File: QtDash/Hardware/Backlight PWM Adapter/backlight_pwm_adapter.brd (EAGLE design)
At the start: 40.4 x 19.5 mm, 9 parts, among them Q1 310mA/60V/1.6Ω, Q2 310mA/60V/1.6Ω

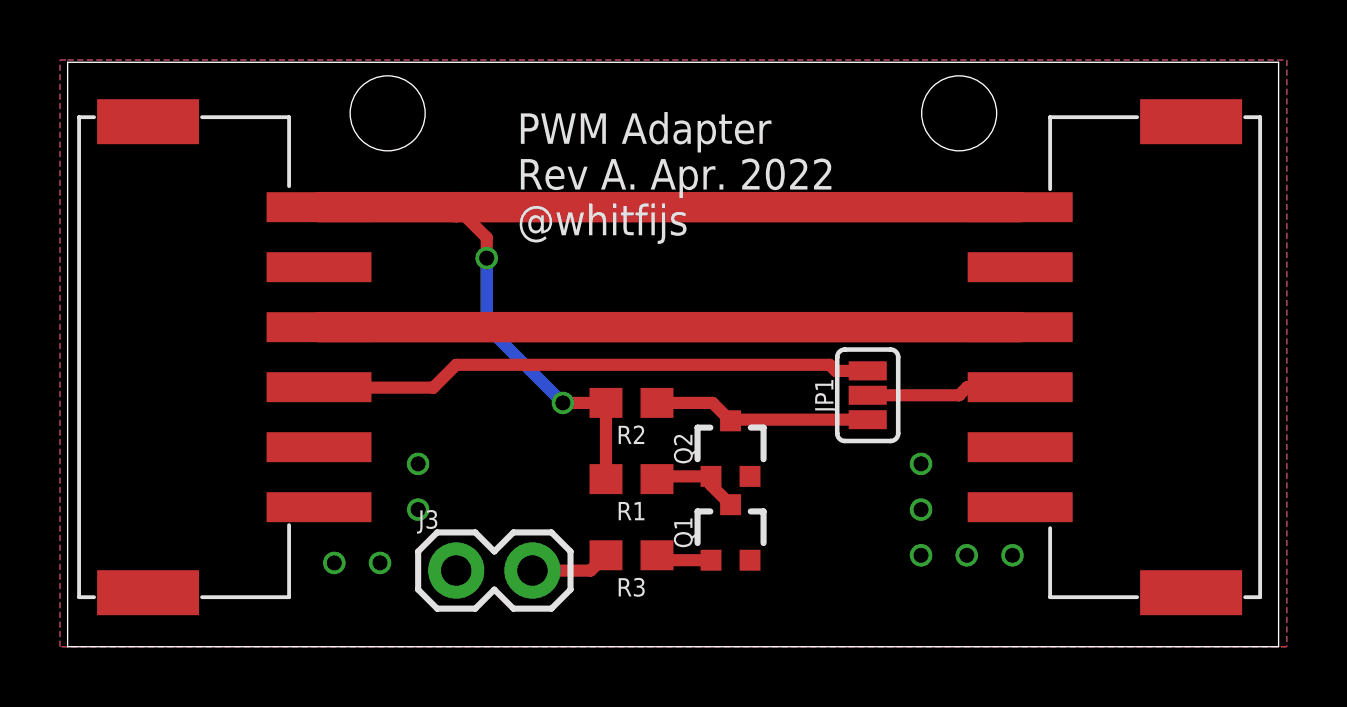
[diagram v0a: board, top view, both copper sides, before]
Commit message: topic/backlight-pwm-control: 	- changed PWM frequency to 30kHz 	- renamed pwm.hpp -> pwm.h 	- started on rev b of PWM adapter board -- pwm signal used directly on EN pin of the OCX OC6700.  There is brightness control that is done outside of the backlight as well that I can't control with the PWM alone.
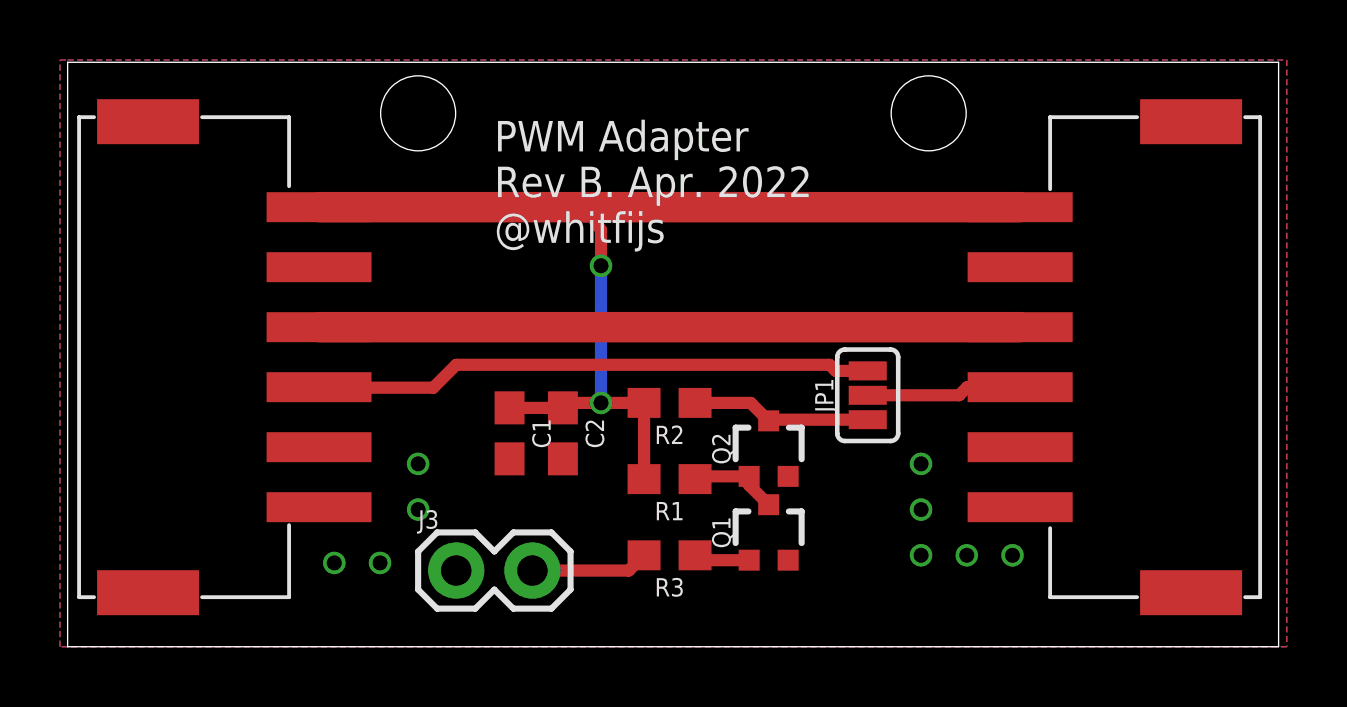
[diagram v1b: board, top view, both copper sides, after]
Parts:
- added C1: 100n, digital_dash:0603
- added C2: 1u, digital_dash:0603
- moved Q1 1.27 mm to (23.6, 3.81)
- moved Q2 1.27 mm to (23.6, 6.60)
- moved R1 1.27 mm to (20.3, 5.59)
- moved R2 1.27 mm to (20.3, 8.13)
- moved R3 1.27 mm to (20.3, 3.05)
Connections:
- net 5V: now also C1.1, C2.1
- net GND: now also C1.2, C2.2
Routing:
- net 5V: track 35.3 -> 37.2 mm
- net PI_PWM_OUT: track 7.29 -> 6.02 mm
- net N$1: track 2.66 -> 3.93 mm
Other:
- board text added: "PWM Adapter Rev B. Apr. 2022 @whitfijs"
- board text removed: "PWM Adapter Rev A. Apr. 2022 @whitfijs"
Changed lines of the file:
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@@
 <setting verticaltext="up"/>
 </settings>
-<grid distance="10" unitdist="mil" unit="mm" style="lines" multiple="1" display="yes" altdistance="0.025" altunitdist="inch" altunit="inch"/>
+<grid distance="10" unitdist="mil" unit="mil" style="lines" multiple="1" display="yes" altdistance="0.025" altunitdist="inch" altunit="inch"/>
 <layers>
 <layer number="1" name="Top" color="4" fill="1" visible="yes" active="yes"/>
@@
 <wire x1="40.62" y1="19.482" x2="0.254" y2="19.482" width="0" layer="20"/>
 <wire x1="0.254" y1="19.482" x2="0.254" y2="0" width="0" layer="20"/>
-<hole x="10.922" y="17.78" drill="2.5"/>
-<hole x="29.972" y="17.78" drill="2.5"/>
-<circle x="10.922" y="17.78" radius="1.27" width="0.4064" layer="41"/>
-<circle x="10.922" y="17.78" radius="1.27" width="0.4064" layer="42"/>
-<circle x="29.972" y="17.78" radius="1.27" width="0.4064" layer="42"/>
-<circle x="29.972" y="17.78" radius="1.27" width="0.4064" layer="41"/>
-<text x="15.24" y="13.716" size="1.016" layer="21" font="vector" ratio="15">PWM Adapter
-Rev A. Apr. 2022
+<hole x="11.938" y="17.78" drill="2.5"/>
+<hole x="28.956" y="17.78" drill="2.5"/>
+<circle x="11.938" y="17.78" radius="1.27" width="0.4064" layer="41"/>
+<circle x="11.938" y="17.78" radius="1.27" width="0.4064" layer="42"/>
+<circle x="28.956" y="17.78" radius="1.27" width="0.4064" layer="42"/>
+<circle x="28.956" y="17.78" radius="1.27" width="0.4064" layer="41"/>
+<text x="14.478" y="13.462" size="1.016" layer="21" font="vector" ratio="15">PWM Adapter
+Rev B. Apr. 2022
 @whitfijs</text>
 </plain>
@@
 <element name="J2" library="backlight_pwm_adapter" package="140-506-417-060" value="" x="32.004" y="9.652" rot="R270"/>
 <element name="JP1" library="SparkFun-Jumpers" package="SMT-JUMPER_3_NO_SILK" value="JUMPER-SMT_3_NO_SILK" x="26.924" y="8.382" rot="R90"/>
-<element name="Q1" library="SparkFun-DiscreteSemi" package="SOT323" value="310mA/60V/1.6Ω" x="22.352" y="3.81">
-<attribute name="PROD_ID" value="TRANS-11151" x="22.352" y="3.81" size="1.778" layer="27" display="off"/>
+<element name="Q1" library="SparkFun-DiscreteSemi" package="SOT323" value="310mA/60V/1.6Ω" x="23.622" y="3.81">
+<attribute name="PROD_ID" value="TRANS-11151" x="23.622" y="3.81" size="1.778" layer="27" display="off"/>
 </element>
-<element name="Q2" library="SparkFun-DiscreteSemi" package="SOT323" value="310mA/60V/1.6Ω" x="22.352" y="6.604">
-<attribute name="PROD_ID" value="TRANS-11151" x="22.352" y="6.604" size="1.778" layer="27" display="off"/>
+<element name="Q2" library="SparkFun-DiscreteSemi" package="SOT323" value="310mA/60V/1.6Ω" x="23.622" y="6.604">
+<attribute name="PROD_ID" value="TRANS-11151" x="23.622" y="6.604" size="1.778" layer="27" display="off"/>
 </element>
-<element name="R1" library="digital_dash" package="0603" value="1k" x="19.05" y="5.588" rot="R180"/>
-<element name="R2" library="digital_dash" package="0603" value="1k" x="19.05" y="8.128" rot="R180"/>
+<element name="R1" library="digital_dash" package="0603" value="1k" x="20.32" y="5.588" rot="R180"/>
+<element name="R2" library="digital_dash" package="0603" value="1k" x="20.32" y="8.128" rot="R180"/>
 <element name="J3" library="SparkFun-Connectors" package="1X02" value="" x="13.208" y="2.54"/>
-<element name="R3" library="digital_dash" package="0603" value="1k" x="19.05" y="3.048" rot="R180"/>
+<element name="R3" library="digital_dash" package="0603" value="1k" x="20.32" y="3.048" rot="R180"/>
+<element name="C1" library="digital_dash" package="0603" value="100n" x="14.986" y="7.112" rot="R270">
+<attribute name="VOLTAGE" value="50V" x="14.986" y="7.112" size="1.778" layer="27" rot="R270" display="off"/>
+</element>
+<element name="C2" library="digital_dash" package="0603" value="1u" x="16.764" y="7.112" rot="R270">
+<attribute name="VOLTAGE" value="25V" x="16.764" y="7.112" size="1.778" layer="27" rot="R270" display="off"/>
+</element>
 </elements>
 <signals>
@@
 <contactref element="R1" pad="1"/>
 <contactref element="Q1" pad="3"/>
-<wire x1="22.352" y1="4.735" x2="21.702" y2="5.385" width="0.4064" layer="1"/>
-<wire x1="21.702" y1="5.385" x2="21.702" y2="5.679" width="0.4064" layer="1"/>
-<wire x1="19.9" y1="5.588" x2="19.991" y2="5.679" width="0.4064" layer="1"/>
-<wire x1="19.991" y1="5.679" x2="21.702" y2="5.679" width="0.4064" layer="1"/>
+<wire x1="23.622" y1="4.735" x2="22.972" y2="5.385" width="0.4064" layer="1"/>
+<wire x1="22.972" y1="5.385" x2="22.972" y2="5.679" width="0.4064" layer="1"/>
+<wire x1="21.17" y1="5.588" x2="21.261" y2="5.679" width="0.4064" layer="1"/>
+<wire x1="21.261" y1="5.679" x2="22.972" y2="5.679" width="0.4064" layer="1"/>
 </signal>
 <signal name="GND">
@@
 <via x="10.668" y="2.794" extent="1-16" drill="0.5"/>
 <via x="9.144" y="2.794" extent="1-16" drill="0.5"/>
+<contactref element="C2" pad="2"/>
+<contactref element="C1" pad="2"/>
 </signal>
 <signal name="PI_PWM_OUT">
@@
 <contactref element="R2" pad="1"/>
 <contactref element="JP1" pad="1"/>
-<wire x1="22.352" y1="7.529" x2="21.753" y2="8.128" width="0.4064" layer="1"/>
-<wire x1="21.753" y1="8.128" x2="19.9" y2="8.128" width="0.4064" layer="1"/>
-<wire x1="22.352" y1="7.529" x2="22.3922" y2="7.5692" width="0.4064" layer="1"/>
-<wire x1="22.3922" y1="7.5692" x2="26.924" y2="7.5692" width="0.4064" layer="1"/>
+<wire x1="23.622" y1="7.529" x2="23.023" y2="8.128" width="0.4064" layer="1"/>
+<wire x1="23.023" y1="8.128" x2="21.17" y2="8.128" width="0.4064" layer="1"/>
+<wire x1="23.622" y1="7.529" x2="23.6622" y2="7.5692" width="0.4064" layer="1"/>
+<wire x1="23.6622" y1="7.5692" x2="26.924" y2="7.5692" width="0.4064" layer="1"/>
 </signal>
 <signal name="5V">
@@
 <contactref element="J2" pad="6"/>
 <contactref element="J1" pad="1"/>
-<wire x1="8.636" y1="14.652" x2="13.208" y2="14.652" width="1.016" layer="1"/>
-<wire x1="13.208" y1="14.652" x2="32.004" y2="14.652" width="1.016" layer="1"/>
-<wire x1="18.2" y1="5.588" x2="18.2" y2="8.128" width="0.4064" layer="1"/>
-<wire x1="18.2" y1="8.128" x2="16.764" y2="8.128" width="0.4064" layer="1"/>
-<via x="16.764" y="8.128" extent="1-16" drill="0.5"/>
-<wire x1="16.764" y1="8.128" x2="14.224" y2="10.668" width="0.4064" layer="16"/>
-<wire x1="14.224" y1="10.668" x2="14.224" y2="12.954" width="0.4064" layer="16"/>
-<via x="14.224" y="12.954" extent="1-16" drill="0.5"/>
-<wire x1="14.224" y1="12.954" x2="14.224" y2="13.636" width="0.4064" layer="1"/>
-<wire x1="14.224" y1="13.636" x2="13.208" y2="14.652" width="0.4064" layer="1"/>
+<wire x1="8.636" y1="14.652" x2="17.526" y2="14.652" width="1.016" layer="1"/>
+<wire x1="17.526" y1="14.652" x2="32.004" y2="14.652" width="1.016" layer="1"/>
+<wire x1="19.47" y1="5.588" x2="19.47" y2="8.128" width="0.4064" layer="1"/>
+<wire x1="19.47" y1="8.128" x2="18.034" y2="8.128" width="0.4064" layer="1"/>
+<via x="18.034" y="8.128" extent="1-16" drill="0.5"/>
+<wire x1="18.034" y1="8.128" x2="18.034" y2="12.7" width="0.4064" layer="16"/>
+<via x="18.034" y="12.7" extent="1-16" drill="0.5"/>
+<wire x1="18.034" y1="12.7" x2="18.034" y2="13.89" width="0.4064" layer="1"/>
+<wire x1="18.034" y1="13.89" x2="17.526" y2="14.652" width="0.4064" layer="1"/>
+<contactref element="C2" pad="1"/>
+<contactref element="C1" pad="1"/>
+<wire x1="18.034" y1="8.128" x2="16.764" y2="8.128" width="0.4064" layer="1"/>
+<wire x1="16.764" y1="8.128" x2="16.764" y2="7.962" width="0.4064" layer="1"/>
+<wire x1="16.764" y1="7.962" x2="14.986" y2="7.962" width="0.4064" layer="1"/>
 </signal>
 <signal name="3.3V">
@@
 <contactref element="J3" pad="2"/>
 <contactref element="R3" pad="2"/>
-<wire x1="15.748" y1="2.54" x2="17.692" y2="2.54" width="0.4064" layer="1"/>
-<wire x1="17.692" y1="2.54" x2="18.2" y2="3.048" width="0.4064" layer="1"/>
+<wire x1="15.748" y1="2.54" x2="18.962" y2="2.54" width="0.4064" layer="1"/>
+<wire x1="18.962" y1="2.54" x2="19.47" y2="3.048" width="0.4064" layer="1"/>
 </signal>
 <signal name="N$2">
 <contactref element="Q1" pad="1"/>
 <contactref element="R3" pad="1"/>
-<wire x1="21.702" y1="2.885" x2="20.063" y2="2.885" width="0.4064" layer="1"/>
-<wire x1="20.063" y1="2.885" x2="19.9" y2="3.048" width="0.4064" layer="1"/>
+<wire x1="22.972" y1="2.885" x2="21.333" y2="2.885" width="0.4064" layer="1"/>
+<wire x1="21.333" y1="2.885" x2="21.17" y2="3.048" width="0.4064" layer="1"/>
 </signal>
 </signals>

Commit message: topic/backlight-pwm-control: 	- added (weak) pullup on PWM input to PWM adapter board 	- probably just need to make a backlight driver on the main board
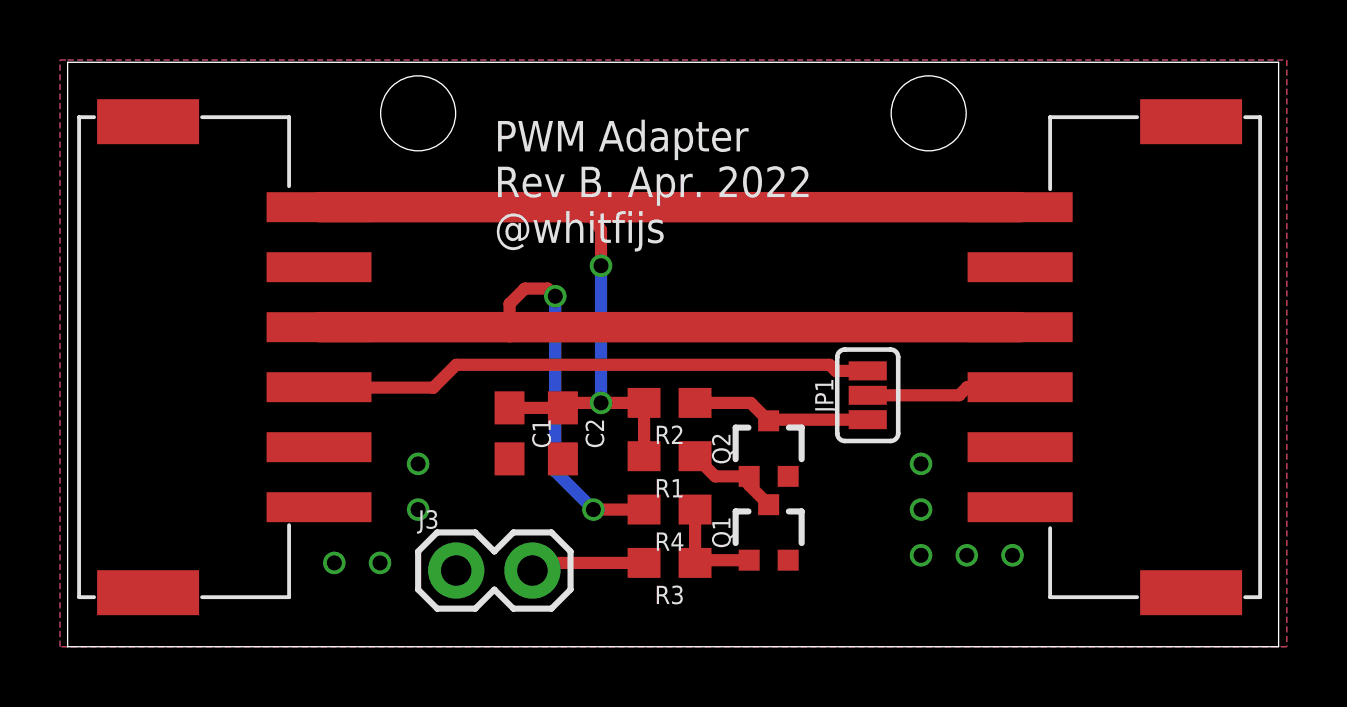
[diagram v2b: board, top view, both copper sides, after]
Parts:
- added R4: 20k, digital_dash:0603
- R3: value 1k -> 100R
- moved R1 0.76 mm to (20.3, 6.35)
- moved R3 0.25 mm to (20.3, 2.79)
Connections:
- net 3.3V: now also R4.2
- net N$2: now also R4.1
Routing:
- net 3.3V: track 23.4 -> 35.3 mm, vias 0 -> 2
- net N$2: track 1.87 -> 3.56 mm
- net 5V: track 37.2 -> 36.5 mm
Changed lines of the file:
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@@
 <attribute name="PROD_ID" value="TRANS-11151" x="23.622" y="6.604" size="1.778" layer="27" display="off"/>
 </element>
-<element name="R1" library="digital_dash" package="0603" value="1k" x="20.32" y="5.588" rot="R180"/>
+<element name="R1" library="digital_dash" package="0603" value="1k" x="20.32" y="6.35" rot="R180"/>
 <element name="R2" library="digital_dash" package="0603" value="1k" x="20.32" y="8.128" rot="R180"/>
 <element name="J3" library="SparkFun-Connectors" package="1X02" value="" x="13.208" y="2.54"/>
-<element name="R3" library="digital_dash" package="0603" value="1k" x="20.32" y="3.048" rot="R180"/>
+<element name="R3" library="digital_dash" package="0603" value="100R" x="20.32" y="2.794" rot="R180"/>
 <element name="C1" library="digital_dash" package="0603" value="100n" x="14.986" y="7.112" rot="R270">
 <attribute name="VOLTAGE" value="50V" x="14.986" y="7.112" size="1.778" layer="27" rot="R270" display="off"/>
@@
 <attribute name="VOLTAGE" value="25V" x="16.764" y="7.112" size="1.778" layer="27" rot="R270" display="off"/>
 </element>
+<element name="R4" library="digital_dash" package="0603" value="20k" x="20.32" y="4.572" rot="R180"/>
 </elements>
 <signals>
@@
 <wire x1="23.622" y1="4.735" x2="22.972" y2="5.385" width="0.4064" layer="1"/>
 <wire x1="22.972" y1="5.385" x2="22.972" y2="5.679" width="0.4064" layer="1"/>
-<wire x1="21.17" y1="5.588" x2="21.261" y2="5.679" width="0.4064" layer="1"/>
-<wire x1="21.261" y1="5.679" x2="22.972" y2="5.679" width="0.4064" layer="1"/>
+<wire x1="21.17" y1="6.35" x2="21.841" y2="5.679" width="0.4064" layer="1"/>
+<wire x1="21.841" y1="5.679" x2="22.972" y2="5.679" width="0.4064" layer="1"/>
 </signal>
 <signal name="GND">
@@
 <wire x1="8.636" y1="14.652" x2="17.526" y2="14.652" width="1.016" layer="1"/>
 <wire x1="17.526" y1="14.652" x2="32.004" y2="14.652" width="1.016" layer="1"/>
-<wire x1="19.47" y1="5.588" x2="19.47" y2="8.128" width="0.4064" layer="1"/>
 <wire x1="19.47" y1="8.128" x2="18.034" y2="8.128" width="0.4064" layer="1"/>
 <via x="18.034" y="8.128" extent="1-16" drill="0.5"/>
@@
 <wire x1="16.764" y1="8.128" x2="16.764" y2="7.962" width="0.4064" layer="1"/>
 <wire x1="16.764" y1="7.962" x2="14.986" y2="7.962" width="0.4064" layer="1"/>
+<wire x1="19.47" y1="6.35" x2="19.47" y2="8.128" width="0.4064" layer="1"/>
 </signal>
 <signal name="3.3V">
 <contactref element="J2" pad="4"/>
 <contactref element="J1" pad="3"/>
-<wire x1="8.636" y1="10.652" x2="32.004" y2="10.652" width="1.016" layer="1"/>
+<wire x1="8.636" y1="10.652" x2="14.986" y2="10.652" width="1.016" layer="1"/>
+<contactref element="R4" pad="2"/>
+<wire x1="14.986" y1="10.652" x2="32.004" y2="10.652" width="1.016" layer="1"/>
+<wire x1="19.47" y1="4.572" x2="17.78" y2="4.572" width="0.4064" layer="1"/>
+<via x="17.78" y="4.572" extent="1-16" drill="0.5"/>
+<wire x1="17.78" y1="4.572" x2="16.51" y2="5.842" width="0.4064" layer="16"/>
+<wire x1="16.51" y1="5.842" x2="16.51" y2="11.684" width="0.4064" layer="16"/>
+<via x="16.51" y="11.684" extent="1-16" drill="0.5"/>
+<wire x1="16.51" y1="11.684" x2="16.256" y2="11.938" width="0.4064" layer="1"/>
+<wire x1="16.256" y1="11.938" x2="15.494" y2="11.938" width="0.4064" layer="1"/>
+<wire x1="15.494" y1="11.938" x2="14.986" y2="11.43" width="0.4064" layer="1"/>
+<wire x1="14.986" y1="11.43" x2="14.986" y2="10.652" width="0.4064" layer="1"/>
 </signal>
 <signal name="LCD_PWM_IN">
@@
 <contactref element="J3" pad="2"/>
 <contactref element="R3" pad="2"/>
-<wire x1="15.748" y1="2.54" x2="18.962" y2="2.54" width="0.4064" layer="1"/>
-<wire x1="18.962" y1="2.54" x2="19.47" y2="3.048" width="0.4064" layer="1"/>
+<wire x1="15.748" y1="2.54" x2="16.002" y2="2.794" width="0.4064" layer="1"/>
+<wire x1="16.002" y1="2.794" x2="19.47" y2="2.794" width="0.4064" layer="1"/>
 </signal>
 <signal name="N$2">
 <contactref element="Q1" pad="1"/>
 <contactref element="R3" pad="1"/>
-<wire x1="22.972" y1="2.885" x2="21.333" y2="2.885" width="0.4064" layer="1"/>
-<wire x1="21.333" y1="2.885" x2="21.17" y2="3.048" width="0.4064" layer="1"/>
+<contactref element="R4" pad="1"/>
+<wire x1="21.17" y1="2.794" x2="21.261" y2="2.885" width="0.4064" layer="1"/>
+<wire x1="21.261" y1="2.885" x2="22.972" y2="2.885" width="0.4064" layer="1"/>
+<wire x1="21.261" y1="2.885" x2="21.17" y2="2.976" width="0.4064" layer="1"/>
+<wire x1="21.17" y1="2.976" x2="21.17" y2="4.572" width="0.4064" layer="1"/>
 </signal>
 </signals>
